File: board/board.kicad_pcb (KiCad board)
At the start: 2 copper layers, 25.7 x 34.4 mm, 8 parts, among them J1 Conn_01x02, P1 CONN_01X08, P2 CONN_01X08, SW1 SW_SPDT, U1 DS18B20

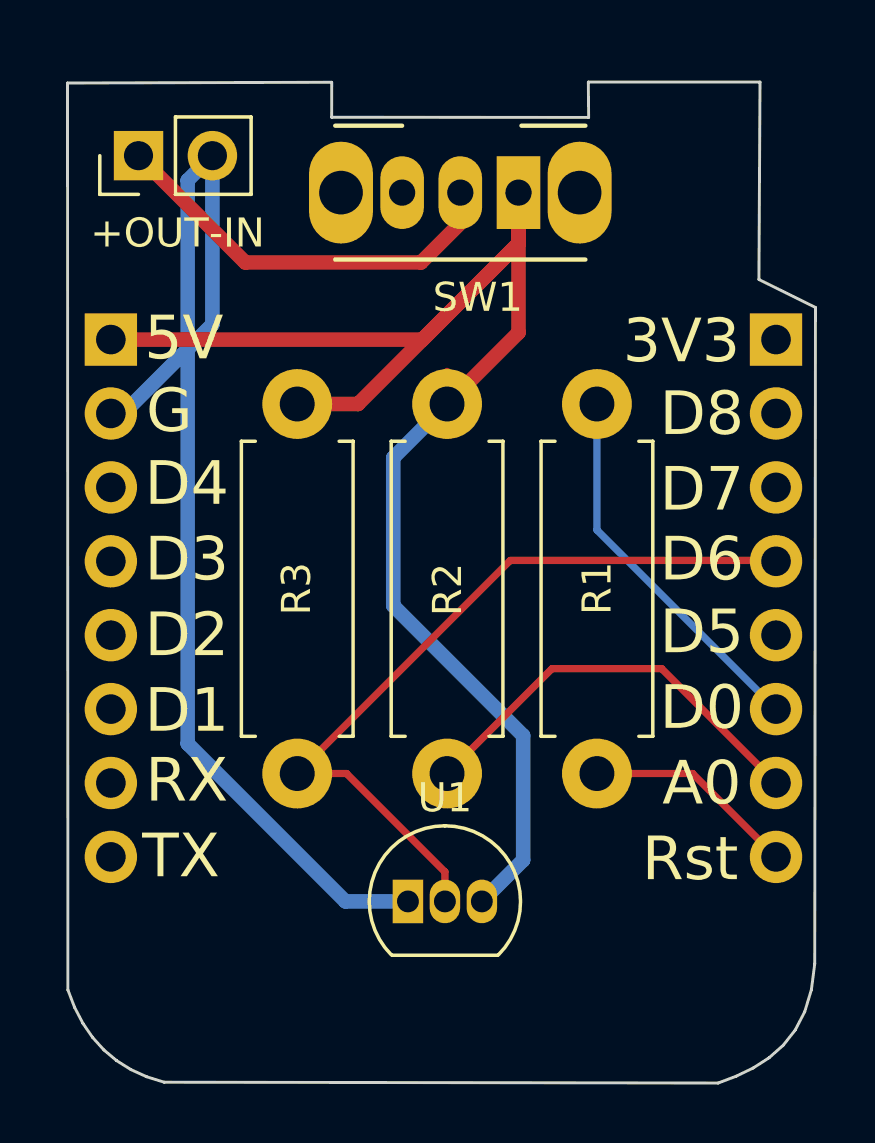
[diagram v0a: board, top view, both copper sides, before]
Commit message: Switch SW1 footprint for actual part.
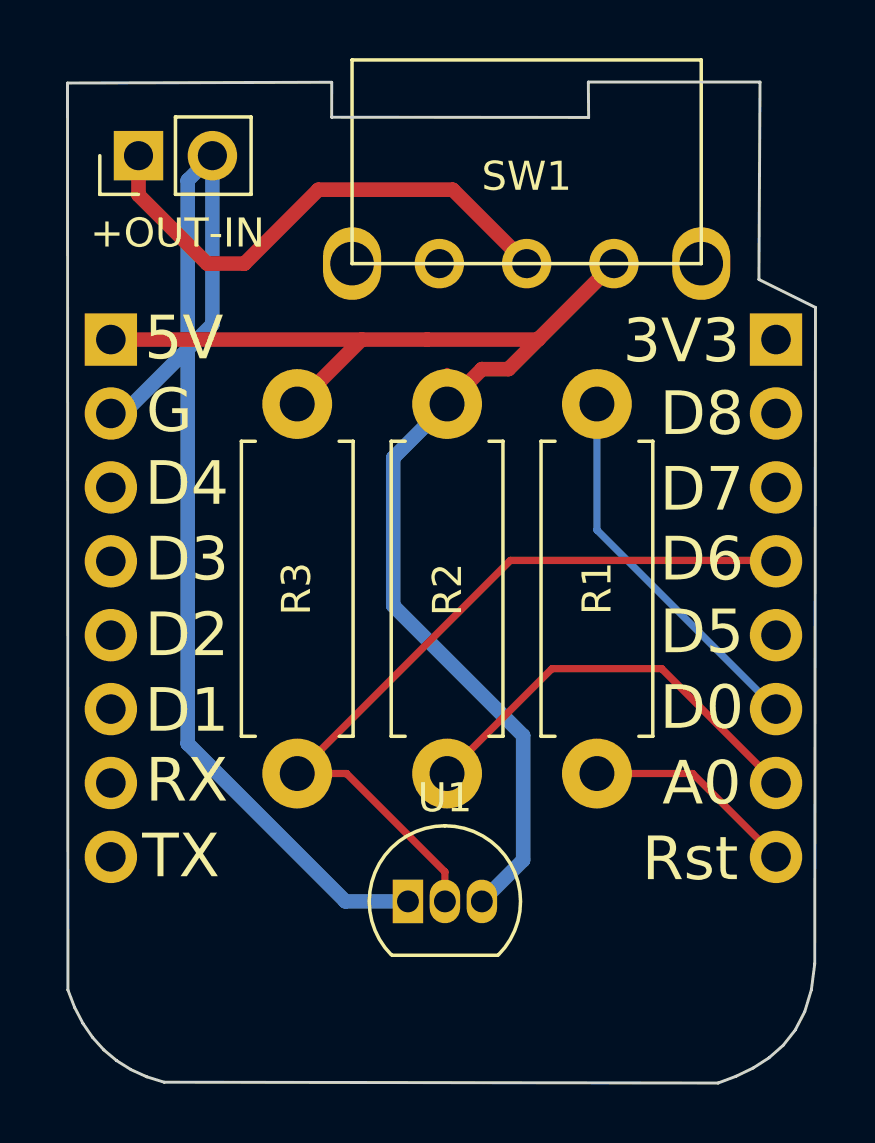
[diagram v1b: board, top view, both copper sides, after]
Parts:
- SW1: footprint Button_Switch_THT:SW_CuK_OS102011MA1QN1_SPDT_Angled -> footprints:SS-12F23-SPDT
- moved SW1 1.10 mm to (141.8, 87.9), turned to 0 degrees
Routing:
- net +5V: track 56.9 -> 49.5 mm
- net +OUT: track 14.5 -> 18.1 mm
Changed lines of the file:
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@@
-(kicad_pcb (version 20171130) (host pcbnew 5.1.6)
+(kicad_pcb (version 20171130) (host pcbnew 5.1.5)
   (general
     (thickness 1.6)
     (drawings 74)
-    (tracks 40)
+    (tracks 43)
     (zones 0)
     (modules 8)
@@
   (page A4)
   (layers
-    (0 F.Cu signal hide)
-    (31 B.Cu signal hide)
+    (0 F.Cu signal)
+    (31 B.Cu signal)
     (32 B.Adhes user)
     (33 F.Adhes user)
@@
     (add_net -IN)
   )
+  (module footprints:SS-12F23-SPDT (layer F.Cu)
+    (at 141.78 87.94)
+    (fp_text reference SW1 (at 0 0.5) (layer F.SilkS)
+      (effects (font (size 1 1) (thickness 0.15)))
+    )
+    (fp_text value SW_SPDT (at 0 -0.5) (layer F.Fab)
+      (effects (font (size 1 1) (thickness 0.15)))
+    )
+    (fp_line (start -6 3.5) (end 6 3.5) (layer F.SilkS) (width 0.12))
+    (fp_line (start 6 3.5) (end 6 -3.5) (layer F.SilkS) (width 0.12))
+    (fp_line (start 6 -3.5) (end -6 -3.5) (layer F.SilkS) (width 0.12))
+    (fp_line (start -6 -3.5) (end -6 3.5) (layer F.SilkS) (width 0.12))
+    (fp_line (start 2 -3.5) (end 2 -6.5) (layer Dwgs.User) (width 0.12))
+    (fp_line (start 2 -6.5) (end 4 -6.5) (layer Dwgs.User) (width 0.12))
+    (fp_line (start 4 -6.5) (end 4 -3.5) (layer Dwgs.User) (width 0.12))
+    (pad 1 thru_hole circle (at 3 3.5) (size 1.7 1.7) (drill 1) (layers *.Cu *.Mask)
+      (net 13 +5V))
+    (pad 2 thru_hole circle (at 0 3.5) (size 1.7 1.7) (drill 1) (layers *.Cu *.Mask)
+      (net 11 +OUT))
+    (pad 3 thru_hole circle (at -3 3.5) (size 1.7 1.7) (drill 1) (layers *.Cu *.Mask)
+      (net 18 "Net-(SW1-Pad3)"))
+    (pad "" thru_hole oval (at 6 3.5) (size 2 2.5) (drill 1.5) (layers *.Cu *.Mask))
+    (pad "" thru_hole oval (at -6 3.5) (size 2 2.5) (drill 1.5) (layers *.Cu *.Mask))
+  )
   (module Resistor_THT:R_Axial_DIN0411_L9.9mm_D3.6mm_P12.70mm_Horizontal (layer F.Cu)
     (at 139.044999 96.265001 270)
@@
       (net 14 D6))
     (model ${KISYS3DMOD}/Resistor_THT.3dshapes/R_Axial_DIN0411_L9.9mm_D3.6mm_P12.70mm_Horizontal.wrl
-      (at (xyz 0 0 0))
-      (scale (xyz 1 1 1))
-      (rotate (xyz 0 0 0))
-    )
-  )
-  (module Button_Switch_THT:SW_CuK_OS102011MA1QN1_SPDT_Angled (layer F.Cu)
-    (at 141.5 89 180)
-    (descr "CuK miniature slide switch, OS series, SPDT, right angle, http://www.ckswitches.com/media/1428/os.pdf")
-    (tags "switch SPDT")
-    (fp_text reference SW1 (at 1.4 -3.6) (layer F.SilkS)
-      (effects (font (size 1 1) (thickness 0.15)))
-    )
-    (fp_text value SW_SPDT (at 1.7 7.7) (layer F.Fab)
-      (effects (font (size 1 1) (thickness 0.15)))
-    )
-    (fp_line (start -3.7 -2.7) (end 7.7 -2.7) (layer F.CrtYd) (width 0.05))
-    (fp_line (start -3.7 6.7) (end -3.7 -2.7) (layer F.CrtYd) (width 0.05))
-    (fp_line (start 7.7 6.7) (end -3.7 6.7) (layer F.CrtYd) (width 0.05))
-    (fp_line (start 7.7 -2.7) (end 7.7 6.7) (layer F.CrtYd) (width 0.05))
-    (fp_line (start 4 2.3) (end 6.3 2.3) (layer F.SilkS) (width 0.15))
-    (fp_line (start -2.3 2.3) (end -0.1 2.3) (layer F.SilkS) (width 0.15))
-    (fp_line (start -2.3 -2.3) (end 6.3 -2.3) (layer F.SilkS) (width 0.15))
-    (fp_line (start 0 6.2) (end 0 2.2) (layer F.Fab) (width 0.1))
-    (fp_line (start 2 6.2) (end 0 6.2) (layer F.Fab) (width 0.1))
-    (fp_line (start 2 2.2) (end 2 6.2) (layer F.Fab) (width 0.1))
-    (fp_line (start 6.3 2.2) (end 6.3 -2.2) (layer F.Fab) (width 0.1))
-    (fp_line (start -2.3 2.2) (end 6.3 2.2) (layer F.Fab) (width 0.1))
-    (fp_line (start -2.3 -2.2) (end -2.3 2.2) (layer F.Fab) (width 0.1))
-    (fp_line (start -2.3 -2.2) (end 6.3 -2.2) (layer F.Fab) (width 0.1))
-    (fp_text user %R (at 2.3 1.7) (layer F.Fab)
-      (effects (font (size 0.5 0.5) (thickness 0.1)))
-    )
-    (pad 1 thru_hole rect (at 0 0 180) (size 1.5 2.5) (drill 0.9) (layers *.Cu *.Mask)
-      (net 13 +5V))
-    (pad 2 thru_hole oval (at 2 0 180) (size 1.5 2.5) (drill 0.9) (layers *.Cu *.Mask)
-      (net 11 +OUT))
-    (pad 3 thru_hole oval (at 4 0 180) (size 1.5 2.5) (drill 0.9) (layers *.Cu *.Mask)
-      (net 18 "Net-(SW1-Pad3)"))
-    (pad "" thru_hole oval (at -2.1 0 180) (size 2.2 3.5) (drill 1.5) (layers *.Cu *.Mask))
-    (pad "" thru_hole oval (at 6.1 0 180) (size 2.2 3.5) (drill 1.5) (layers *.Cu *.Mask))
-    (model ${KISYS3DMOD}/Button_Switch_THT.3dshapes/SW_CuK_OS102011MA1QN1_SPDT_Angled.wrl
       (at (xyz 0 0 0))
       (scale (xyz 1 1 1))
@@
   (gr_line (start 149.8 85.2) (end 143.9 85.2) (layer Edge.Cuts) (width 0.1))
   (segment (start 128.44 87.73) (end 128.44 88.07) (width 0.25) (layer F.Cu) (net 11))
-  (segment (start 139.5 90.05) (end 139.5 89) (width 0.5) (layer F.Cu) (net 11))
-  (segment (start 138.14999 91.40001) (end 139.5 90.05) (width 0.5) (layer F.Cu) (net 11))
-  (segment (start 132.11001 91.40001) (end 138.14999 91.40001) (width 0.5) (layer F.Cu) (net 11))
-  (segment (start 128.44 87.73) (end 132.11001 91.40001) (width 0.5) (layer F.Cu) (net 11))
+  (segment (start 128.44 89.08) (end 130.8 91.44) (width 0.5) (layer F.Cu) (net 11))
+  (segment (start 128.44 87.73) (end 128.44 89.08) (width 0.5) (layer F.Cu) (net 11))
+  (segment (start 130.8 91.44) (end 132.08 91.44) (width 0.5) (layer F.Cu) (net 11))
+  (segment (start 132.08 91.44) (end 134.62 88.9) (width 0.5) (layer F.Cu) (net 11))
+  (segment (start 139.24 88.9) (end 141.78 91.44) (width 0.5) (layer F.Cu) (net 11))
+  (segment (start 134.62 88.9) (end 139.24 88.9) (width 0.5) (layer F.Cu) (net 11))
   (segment (start 127.920002 96.59) (end 127.49 96.59) (width 0.5) (layer B.Cu) (net 12))
   (segment (start 130.98 93.530002) (end 127.920002 96.59) (width 0.5) (layer B.Cu) (net 12))
@@
   (segment (start 140.22 113.187095) (end 140.22 113.03) (width 0.25) (layer B.Cu) (net 13))
   (segment (start 139.044999 96.265001) (end 139.044999 95.144999) (width 0.25) (layer F.Cu) (net 13))
-  (segment (start 138.2 94.05) (end 127.49 94.05) (width 0.5) (layer F.Cu) (net 13))
-  (segment (start 141.5 90.75) (end 138.2 94.05) (width 0.5) (layer F.Cu) (net 13))
-  (segment (start 135.984999 96.265001) (end 133.894999 96.265001) (width 0.5) (layer F.Cu) (net 13))
-  (segment (start 141.5 90.75) (end 135.984999 96.265001) (width 0.5) (layer F.Cu) (net 13))
-  (segment (start 141.5 89) (end 141.5 90.75) (width 0.5) (layer F.Cu) (net 13))
-  (segment (start 141.5 93.81) (end 141.5 89) (width 0.5) (layer F.Cu) (net 13))
-  (segment (start 139.044999 96.265001) (end 141.5 93.81) (width 0.5) (layer F.Cu) (net 13))
   (segment (start 137.194998 103.194998) (end 141.66 107.66) (width 0.5) (layer B.Cu) (net 13))
   (segment (start 137.194998 98.115002) (end 137.194998 103.194998) (width 0.5) (layer B.Cu) (net 13))
@@
   (segment (start 141.66 111.94) (end 140.24 113.36) (width 0.5) (layer B.Cu) (net 13))
   (segment (start 141.66 107.66) (end 141.66 111.94) (width 0.5) (layer B.Cu) (net 13))
+  (segment (start 142.17 94.05) (end 144.78 91.44) (width 0.5) (layer F.Cu) (net 13))
+  (segment (start 140.244998 95.065002) (end 141.154998 95.065002) (width 0.5) (layer F.Cu) (net 13))
+  (segment (start 139.044999 96.265001) (end 140.244998 95.065002) (width 0.5) (layer F.Cu) (net 13))
+  (segment (start 141.154998 95.065002) (end 142.24 93.98) (width 0.5) (layer F.Cu) (net 13))
+  (segment (start 136.11 94.05) (end 133.894999 96.265001) (width 0.5) (layer F.Cu) (net 13))
+  (segment (start 138.36 94.05) (end 136.11 94.05) (width 0.25) (layer F.Cu) (net 13))
+  (segment (start 127.49 94.05) (end 138.36 94.05) (width 0.5) (layer F.Cu) (net 13))
+  (segment (start 138.36 94.05) (end 142.17 94.05) (width 0.5) (layer F.Cu) (net 13))
   (segment (start 138.97 112.342946) (end 138.97 113.36) (width 0.25) (layer F.Cu) (net 14))
   (segment (start 135.592055 108.965001) (end 138.97 112.342946) (width 0.25) (layer F.Cu) (net 14))

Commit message: Add JLCJLCJLCJLC to silk screen.
... to make sure JLCPCB place the order number somewhere hidden.
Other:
- board text added: "JLCJLCJLCJLC"
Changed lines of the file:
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@@
   (general
     (thickness 1.6)
-    (drawings 74)
+    (drawings 75)
     (tracks 43)
     (zones 0)
@@
     )
   )
+  (gr_text JLCJLCJLCJLC (at 138.938 117.856) (layer B.SilkS)
+    (effects (font (size 1 1) (thickness 0.15)) (justify mirror))
+  )
   (gr_text +OUT-IN (at 129.78 90.39) (layer F.SilkS)
